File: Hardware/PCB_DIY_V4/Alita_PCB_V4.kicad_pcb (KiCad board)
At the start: 2 copper layers, 100 x 55 mm, 0 parts

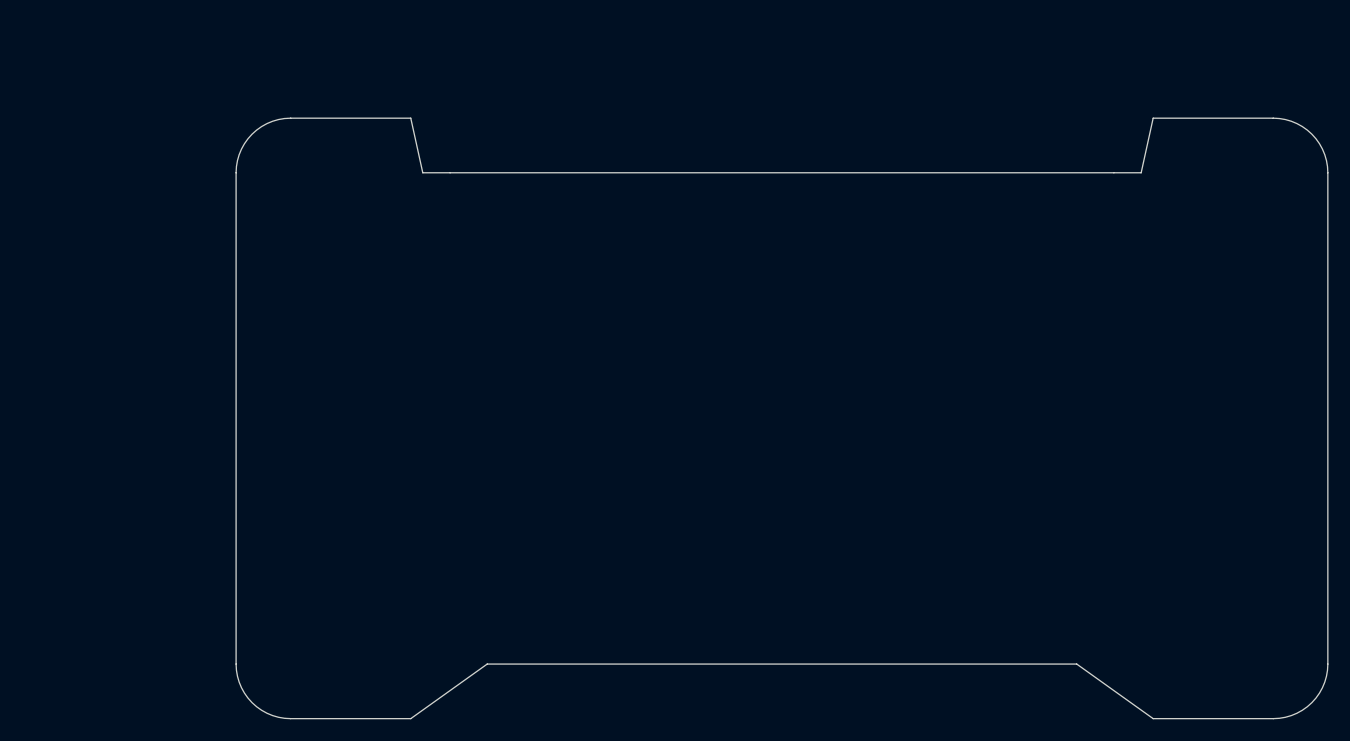
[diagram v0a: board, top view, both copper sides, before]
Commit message: Asignacion de huellas
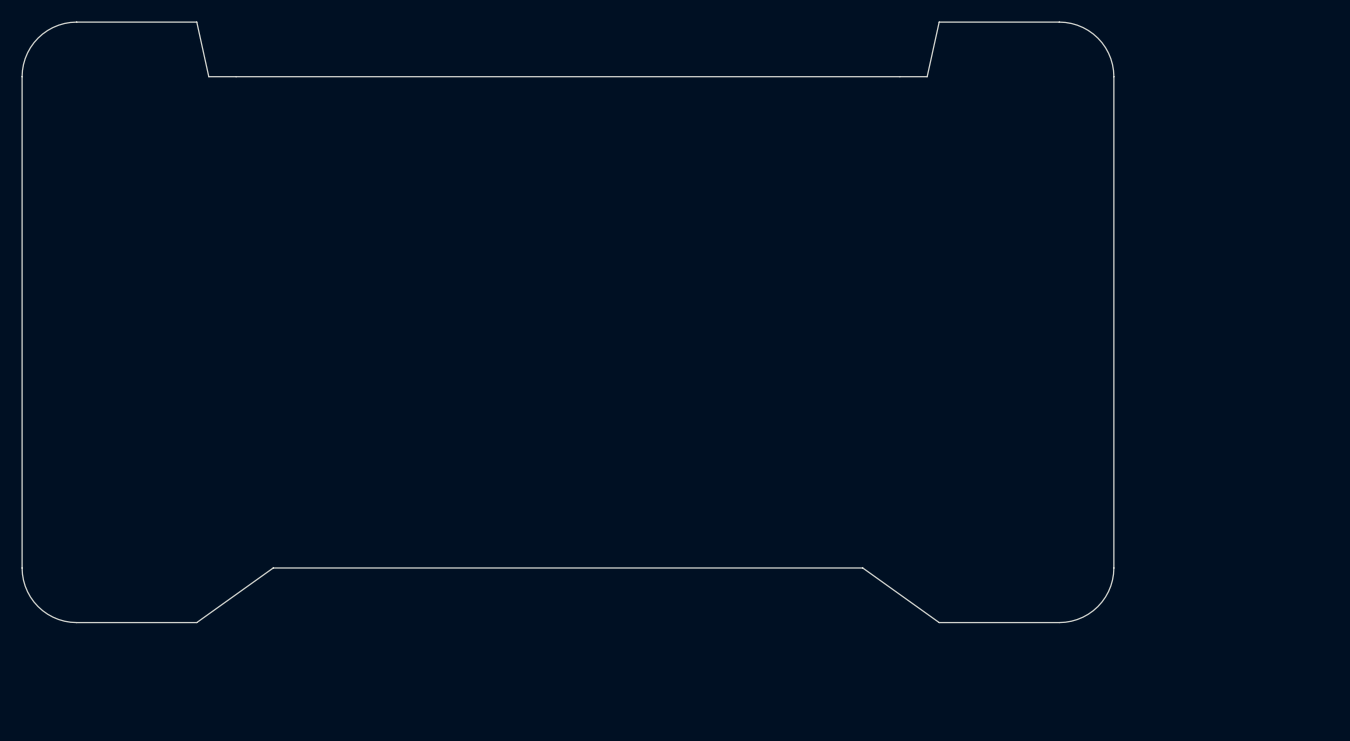
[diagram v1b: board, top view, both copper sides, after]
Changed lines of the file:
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@@
 	(net 0 "")
 	(gr_line
-		(start 34.8 27.8)
-		(end 34.8 72.8)
+		(start 15.2 19)
+		(end 15.2 64)
 		(stroke
 			(width 0.05)
@@
 	)
 	(gr_line
-		(start 50.8 77.8)
-		(end 39.8 77.8)
+		(start 31.2 69)
+		(end 20.2 69)
 		(stroke
 			(width 0.05)
@@
 	)
 	(gr_line
-		(start 134.8 72.8)
-		(end 134.8 27.8)
+		(start 115.2 64)
+		(end 115.2 19)
 		(stroke
 			(width 0.05)
@@
 	)
 	(gr_arc
-		(start 39.8 77.8)
-		(mid 36.264466 76.335534)
-		(end 34.8 72.8)
+		(start 20.2 69)
+		(mid 16.664466 67.535534)
+		(end 15.2 64)
 		(stroke
 			(width 0.05)
@@
 	)
 	(gr_line
-		(start 57.8 72.8)
-		(end 50.8 77.8)
+		(start 38.2 64)
+		(end 31.2 69)
 		(stroke
 			(width 0.05)
@@
 	)
 	(gr_line
-		(start 54.4 27.8)
-		(end 51.9 27.8)
+		(start 34.8 19)
+		(end 32.3 19)
 		(stroke
 			(width 0.05)
@@
 	)
 	(gr_line
-		(start 57.8 72.8)
-		(end 111.8 72.8)
+		(start 38.2 64)
+		(end 92.2 64)
 		(stroke
 			(width 0.05)
@@
 	)
 	(gr_line
-		(start 51.9 27.8)
-		(end 50.8 22.8)
+		(start 32.3 19)
+		(end 31.2 14)
 		(stroke
 			(width 0.05)
@@
 	)
 	(gr_line
-		(start 111.8 72.8)
-		(end 118.8 77.8)
+		(start 92.2 64)
+		(end 99.2 69)
 		(stroke
 			(width 0.05)
@@
 	)
 	(gr_arc
-		(start 129.8 22.8)
-		(mid 133.335534 24.264466)
-		(end 134.8 27.8)
+		(start 110.2 14)
+		(mid 113.735534 15.464466)
+		(end 115.2 19)
 		(stroke
 			(width 0.05)
@@
 	)
 	(gr_line
-		(start 117.7 27.8)
-		(end 118.8 22.8)
+		(start 98.1 19)
+		(end 99.2 14)
 		(stroke
 			(width 0.05)
@@
 	)
 	(gr_line
-		(start 129.8 22.8)
-		(end 118.8 22.8)
+		(start 110.2 14)
+		(end 99.2 14)
 		(stroke
 			(width 0.05)
@@
 	)
 	(gr_line
-		(start 39.8 22.8)
-		(end 50.8 22.8)
+		(start 20.2 14)
+		(end 31.2 14)
 		(stroke
 			(width 0.05)
@@
 	)
 	(gr_line
-		(start 54.4 27.8)
-		(end 115.2 27.8)
+		(start 34.8 19)
+		(end 95.6 19)
 		(stroke
 			(width 0.05)
@@
 	)
 	(gr_arc
-		(start 34.8 27.8)
-		(mid 36.264466 24.264466)
-		(end 39.8 22.8)
+		(start 15.2 19)
+		(mid 16.664466 15.464466)
+		(end 20.2 14)
 		(stroke
 			(width 0.05)
@@
 	)
 	(gr_arc
-		(start 134.8 72.8)
-		(mid 133.335534 76.335534)
-		(end 129.8 77.8)
+		(start 115.2 64)
+		(mid 113.735534 67.535534)
+		(end 110.2 69)
 		(stroke
 			(width 0.05)
@@
 	)
 	(gr_line
-		(start 129.8 77.8)
-		(end 118.8 77.8)
+		(start 110.2 69)
+		(end 99.2 69)
 		(stroke
 			(width 0.05)
@@
 	)
 	(gr_line
-		(start 115.2 27.8)
-		(end 117.7 27.8)
+		(start 95.6 19)
+		(end 98.1 19)
 		(stroke
 			(width 0.05)

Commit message: Primer posicionamiento de componentes en PCB
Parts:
- added C2: 100nF, Capacitor_SMD:C_0805_2012Metric_Pad1.18x1.45mm_HandSolder, F.Cu at (108.2, 112.4)
- added C3: 100uF, Capacitor_SMD:CP_Elec_5x4.5, F.Cu at (103.0, 107.1)
- added D1: 1N5819, Diode_SMD:D_SMA, F.Cu at (103.0, 101.2)
- added D3: 1N5819, Diode_SMD:D_SMA, F.Cu at (103.0, 113.0)
- added H1: MountingHole, MountingHole:MountingHole_3.2mm_M3_DIN965, F.Cu at (102.0, 87.5)
- added H2: MountingHole, MountingHole:MountingHole_3.2mm_M3_DIN965, F.Cu at (192.0, 87.5)
- added H3: MountingHole, MountingHole:MountingHole_3.2mm_M3_DIN965, F.Cu at (102.0, 132.5)
- added H4: MountingHole, MountingHole:MountingHole_3.2mm_M3_DIN965, F.Cu at (192.0, 132.5)
- added J1: Vss, MixLib:Bornera_2_duo, F.Cu at (103.0, 121.0)
- added J2: MUX_header, Connector_PinHeader_2.54mm:PinHeader_1x16_P2.54mm_Horizontal, F.Cu at (176.6, 126.3)
- added J4: Driver, Connector_PinHeader_2.54mm:PinHeader_1x06_P2.54mm_Horizontal, F.Cu at (194.2, 108.0)
- added J5: Buttons, Connector_Molex:Molex_KK-254_AE-6410-04A_1x04_P2.54mm_Vertical, F.Cu at (168.7, 87.3)
- added J8: Conn_01x03_Pin, Connector_Molex:Molex_KK-254_AE-6410-03A_1x03_P2.54mm_Vertical, F.Cu at (100.5, 95.1)
- added J9: Conn_01x04_Pin, Connector_Molex:Molex_KK-254_AE-6410-04A_1x04_P2.54mm_Vertical, F.Cu at (158.7, 87.3)
- added P1: 5v_Pins, Connector_IDC:IDC-Header_2x05_P2.54mm_Vertical, F.Cu at (159.1, 98.0)
- added P2: 3.3v_Pins, Connector_IDC:IDC-Header_2x05_P2.54mm_Vertical, F.Cu at (182.6, 98.1)
- added R1: 10k, PCM_Resistor_SMD_AKL:R_0805_2012Metric_Pad1.15x1.40mm_HandSolder, F.Cu at (169.8, 92.6)
- added R2: 10k, PCM_Resistor_SMD_AKL:R_0805_2012Metric_Pad1.15x1.40mm_HandSolder, F.Cu at (174.9, 92.6)
- added U1: MUX 4067, MixLib:HP4067_module, F.Cu at (157.4, 115.0)
- added U4: ESP32_NODEMCU, MixLib:Nodemcu_ESP32S_38pin, F.Cu at (122.5, 109.0)
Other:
- outline, holes or cut-outs redrawn

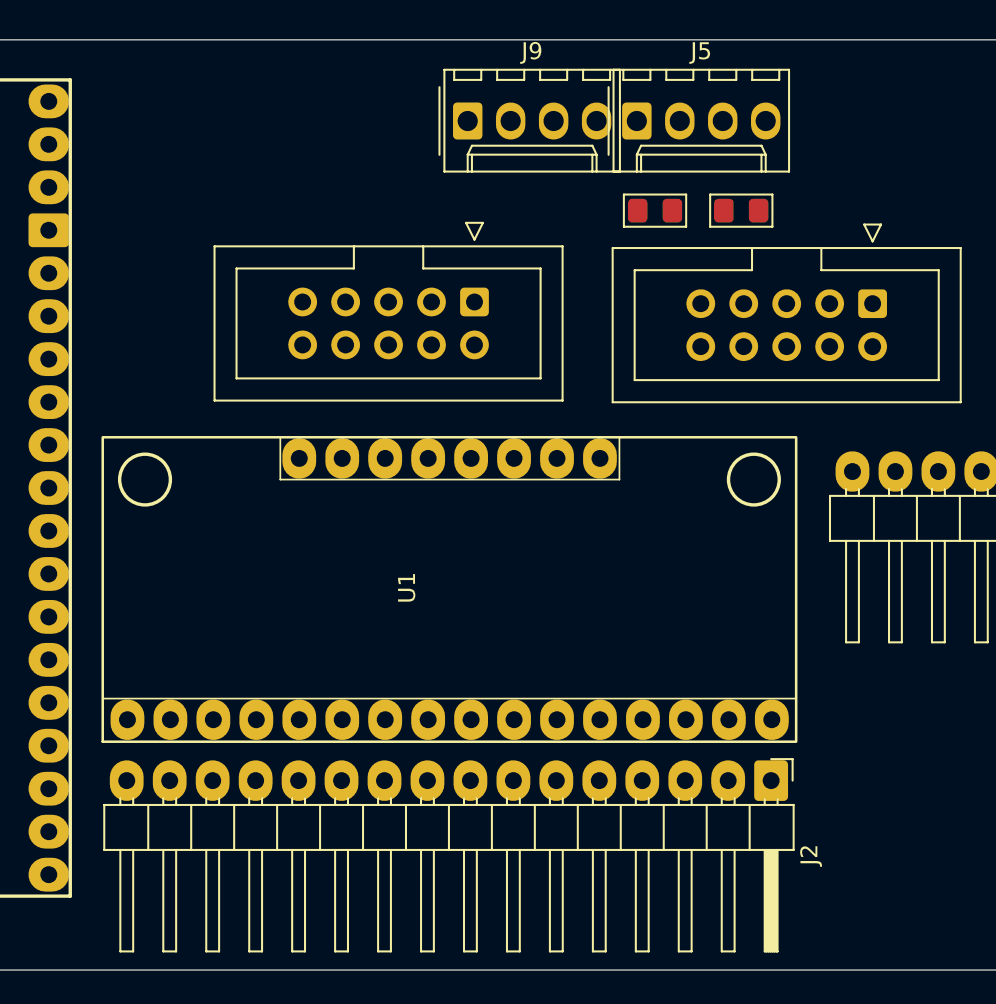
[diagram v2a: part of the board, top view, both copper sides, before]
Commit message: Modificacion de footprint y posicionamiento
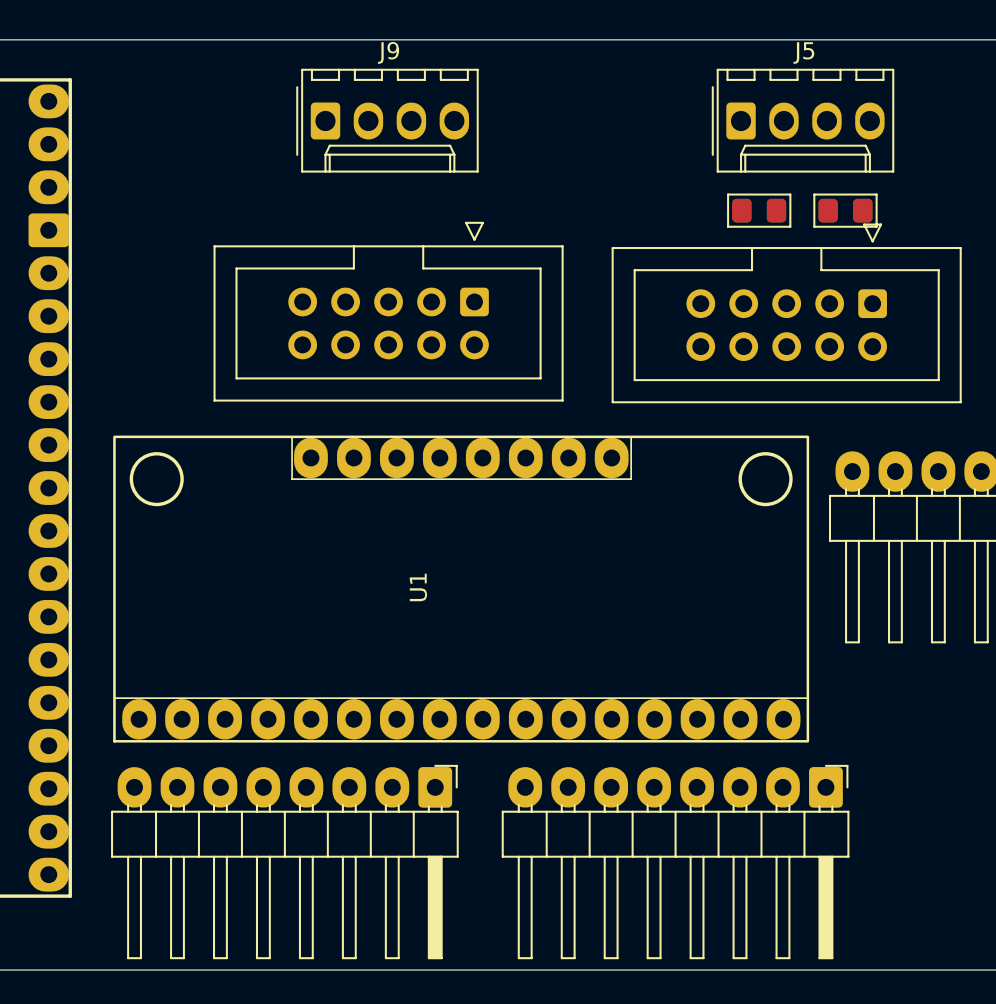
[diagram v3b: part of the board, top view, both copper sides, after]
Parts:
- added J3: MUX_header2, Connector_PinHeader_2.54mm:PinHeader_1x08_P2.54mm_Horizontal, F.Cu at (179.9, 126.7)
- J2: value MUX_header -> MUX_header1; footprint Connector_PinHeader_2.54mm:PinHeader_1x16_P2.54mm_Horizontal -> Connector_PinHeader_2.54mm:PinHeader_1x08_P2.54mm_Horizontal
- moved J2 19.9 mm to (156.8, 126.7)
- moved J9 8.41 mm to (150.3, 87.3)
- moved J5 6.16 mm to (174.9, 87.3)
- moved R1 6.16 mm to (175.9, 92.6)
- moved R2 6.16 mm to (181.0, 92.6)
- moved U1 0.69 mm to (158.1, 114.9)
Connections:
- U1 pad 1: Net-(J2-Pin_1) -> Net-(J3-Pin_1)
- U1 pad 10: Net-(J2-Pin_10) -> Net-(J2-Pin_2)
- U1 pad 11: Net-(J2-Pin_11) -> Net-(J2-Pin_3)
- U1 pad 12: Net-(J2-Pin_12) -> Net-(J2-Pin_4)
- U1 pad 13: Net-(J2-Pin_13) -> Net-(J2-Pin_5)
- U1 pad 14: Net-(J2-Pin_14) -> Net-(J2-Pin_6)
- U1 pad 15: Net-(J2-Pin_15) -> Net-(J2-Pin_7)
- U1 pad 16: Net-(J2-Pin_16) -> Net-(J2-Pin_8)
- U1 pad 2: Net-(J2-Pin_2) -> Net-(J3-Pin_2)
- U1 pad 3: Net-(J2-Pin_3) -> Net-(J3-Pin_3)
- U1 pad 4: Net-(J2-Pin_4) -> Net-(J3-Pin_4)
- U1 pad 5: Net-(J2-Pin_5) -> Net-(J3-Pin_5)
- U1 pad 6: Net-(J2-Pin_6) -> Net-(J3-Pin_6)
- U1 pad 7: Net-(J2-Pin_7) -> Net-(J3-Pin_7)
- U1 pad 8: Net-(J2-Pin_8) -> Net-(J3-Pin_8)
- U1 pad 9: Net-(J2-Pin_9) -> Net-(J2-Pin_1)

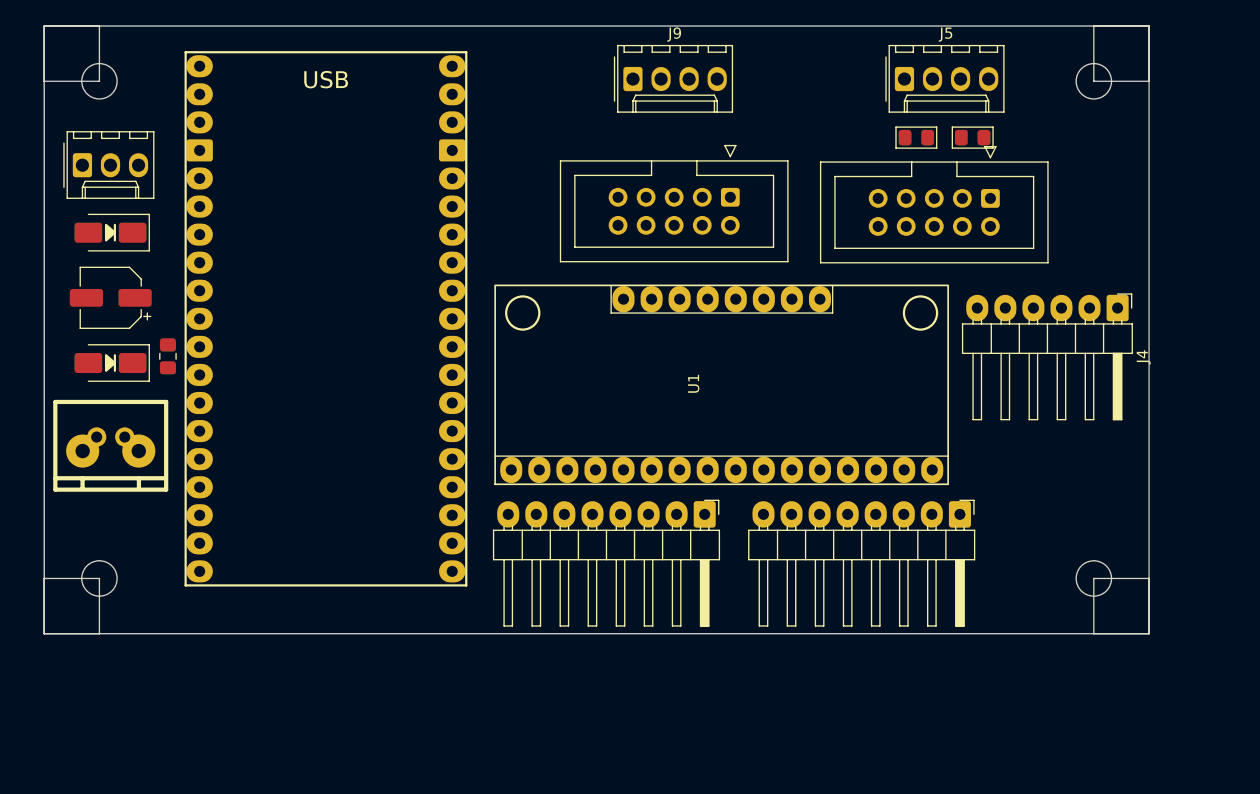
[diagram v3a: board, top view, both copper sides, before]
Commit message: Segundo posicionamiento de componentes y ruteo parcial
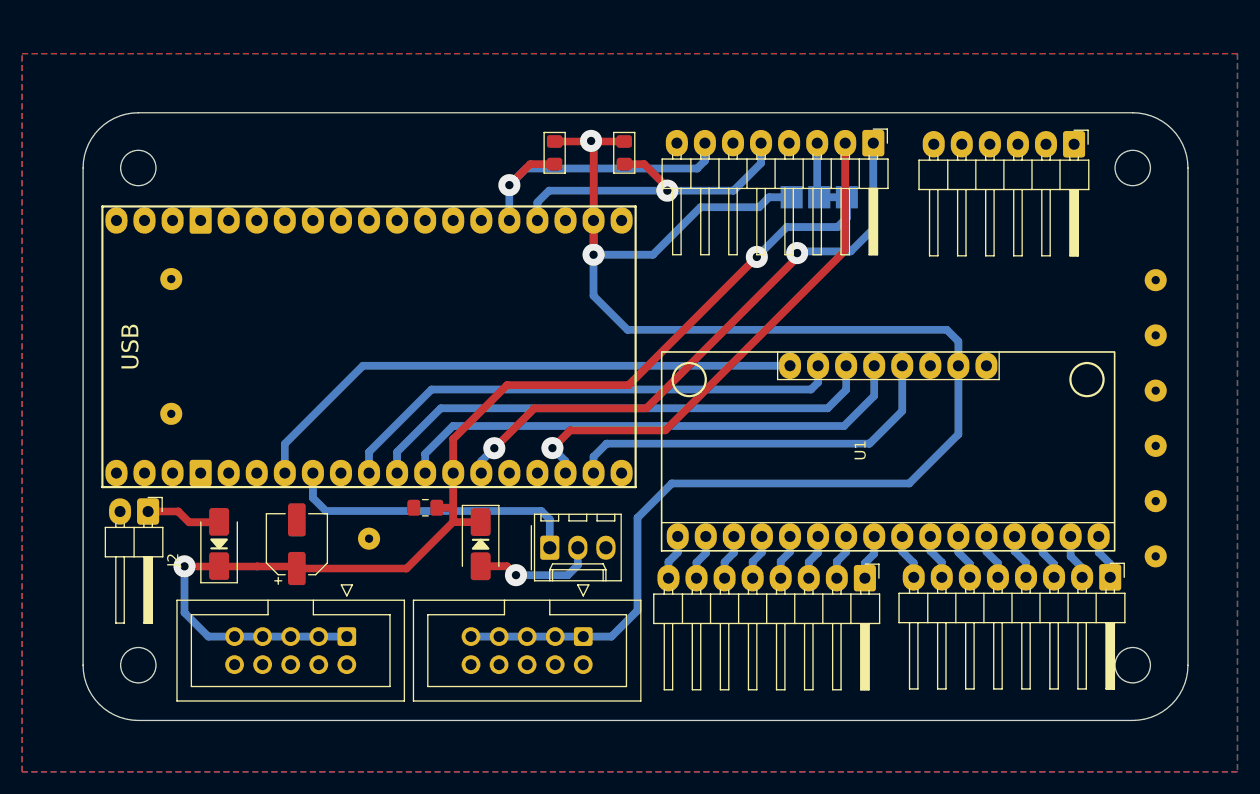
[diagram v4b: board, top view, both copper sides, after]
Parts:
- removed C3: 100uF, Capacitor_SMD:CP_Elec_5x4.5
- removed D3: 1N5819, Diode_SMD:D_SMA
- removed J3: MUX_header2, Connector_PinHeader_2.54mm:PinHeader_1x08_P2.54mm_Horizontal
- removed J8: Conn_01x03_Pin, Connector_Molex:Molex_KK-254_AE-6410-03A_1x03_P2.54mm_Vertical
- removed J9: Conn_01x04_Pin, Connector_Molex:Molex_KK-254_AE-6410-04A_1x04_P2.54mm_Vertical
- removed U4: ESP32_NODEMCU, MixLib:Nodemcu_ESP32S_38pin
- added ?: , , F.Cu at (108.5, 117.6)
- added ?: , , F.Cu at (197.6, 105.5)
- added ?: , , F.Cu at (197.6, 115.5)
- added ?: , , F.Cu at (108.5, 105.4)
- added ?: , , F.Cu at (126.4, 128.9)
- added ?: , , F.Cu at (197.6, 120.5)
- added ?: , , F.Cu at (197.6, 125.5)
- added ?: , , F.Cu at (197.6, 110.5)
- added ?: , , F.Cu at (197.6, 130.5)
- added C1: 100uF, Capacitor_SMD:CP_Elec_5x4.5, F.Cu at (119.9, 129.4)
- added D2: 1N5819, Diode_SMD:D_SMA, F.Cu at (136.5, 129.4)
- added J6: MUX_header1, Connector_PinHeader_2.54mm:PinHeader_1x08_P2.54mm_Horizontal, F.Cu at (171.3, 132.5)
- added J7: MUX_header2, Connector_PinHeader_2.54mm:PinHeader_1x08_P2.54mm_Horizontal, F.Cu at (193.5, 132.4)
- added JP1: OLED_tension, MixLib:SolderJumper-3_Big_Bridged, B.Cu at (167.0, 98.0)
- added U2: ESP32_NODEMCU, MixLib:Nodemcu_ESP32S_38pin, F.Cu at (126.4, 111.5)
- J1: value Vss -> Interface; footprint MixLib:Bornera_2_duo -> Connector_PinHeader_2.54mm:PinHeader_1x08_P2.54mm_Horizontal
- J2: value MUX_header1 -> Vss; footprint Connector_PinHeader_2.54mm:PinHeader_1x08_P2.54mm_Horizontal -> Connector_PinHeader_2.54mm:PinHeader_1x02_P2.54mm_Horizontal
- J4: value Driver -> Conn_01x03_Pin; footprint Connector_PinHeader_2.54mm:PinHeader_1x06_P2.54mm_Horizontal -> Connector_Molex:Molex_KK-254_AE-6410-03A_1x03_P2.54mm_Vertical
- J5: value Buttons -> Driver; footprint Connector_Molex:Molex_KK-254_AE-6410-04A_1x04_P2.54mm_Vertical -> Connector_PinHeader_2.54mm:PinHeader_1x06_P2.54mm_Horizontal
- moved H2 101.4 mm to (105.5, 140.3)
- moved H3 100.6 mm to (195.5, 95.3)
- moved J1 74.4 mm to (172.0, 93.1), turned to -90 degrees
- moved J4 55.8 mm to (142.8, 129.7), turned to 0 degrees
- moved P2 54.1 mm to (145.8, 137.8)
- moved P1 52.8 mm to (124.4, 137.8)
- moved J2 50.4 mm to (106.4, 126.4)
- moved R2 37.9 mm to (143.2, 94.0), turned to -90 degrees
- moved D1 29.8 mm to (112.8, 129.4), turned to 90 degrees
- moved C2 27.0 mm to (131.5, 126.1), turned to 180 degrees
- moved R1 26.5 mm to (149.5, 94.0), turned to -90 degrees
- moved J5 16.4 mm to (190.2, 93.2), turned to -90 degrees
- moved U1 16.2 mm to (173.2, 121.0)
- moved H4 8.60 mm to (195.5, 140.3)
- moved H1 8.60 mm to (105.5, 95.3)
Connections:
- J1 pad 1: Net-(D3-A) -> /SDA
- J1 pad 2: GND -> /SCL
- J2 pad 1: Net-(J2-Pin_1) -> Net-(D1-A)
- J2 pad 2: Net-(J2-Pin_2) -> GND
- J4 pad 1: +5V -> /ESC
- J4 pad 2: /MB2 -> Net-(D2-A)
- J4 pad 3: /MB1 -> GND
- J5 pad 1: /Button1 -> +5V
- J5 pad 2: GND -> /MB2
- J5 pad 3: /Button2 -> /MB1
- J5 pad 4: GND -> /MA2
- P2 pad 1: +3V3 -> +3.3V
- P2 pad 3: +3V3 -> +3.3V
- P2 pad 5: +3V3 -> +3.3V
- P2 pad 7: +3V3 -> +3.3V
- P2 pad 9: +3V3 -> +3.3V
- U1 pad 10: Net-(J2-Pin_2) -> Net-(J7-Pin_7)
- U1 pad 11: Net-(J2-Pin_3) -> Net-(J7-Pin_6)
- U1 pad 12: Net-(J2-Pin_4) -> Net-(J7-Pin_5)
- U1 pad 13: Net-(J2-Pin_5) -> Net-(J7-Pin_4)
- U1 pad 14: Net-(J2-Pin_6) -> Net-(J7-Pin_3)
- U1 pad 15: Net-(J2-Pin_7) -> Net-(J7-Pin_2)
- U1 pad 16: Net-(J2-Pin_8) -> Net-(J7-Pin_1)
- U1 pad 9: Net-(J2-Pin_1) -> Net-(J7-Pin_8)
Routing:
- net +3.3V: track 0.00 -> 142.2 mm, vias 0 -> 2
- net +5V: track 0.00 -> 103.6 mm, vias 0 -> 2
- net /SDA: track 0.00 -> 53.3 mm, vias 0 -> 2
- net /SIG: track 0.00 -> 51.3 mm
- net /S1: track 0.00 -> 47.3 mm
- net /S2: track 0.00 -> 47.0 mm
- net /S3: track 0.00 -> 46.7 mm
- net /SCL: track 0.00 -> 46.4 mm, vias 0 -> 1
- net /S0: track 0.00 -> 35.2 mm
- net /Button1: track 0.00 -> 30.2 mm, vias 0 -> 1
- net /Button2: track 0.00 -> 28.3 mm, vias 0 -> 1
- net /ESC: track 0.00 -> 27.1 mm
- net Net-(D2-A): track 0.00 -> 11.1 mm, vias 0 -> 1
- net Net-(D1-A): track 0.00 -> 6.83 mm
- net Net-(J1-Pin_3): track 0.00 -> 4.98 mm
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- added copper zone on B.Cu, net GND
- added copper zone on F.Cu, net GND
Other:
- outline, holes or cut-outs redrawn
